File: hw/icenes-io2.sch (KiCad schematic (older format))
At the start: 35 parts, among them J3 Conn_02x11_Odd_Even, J4 Conn_02x31_Odd_Even, J5 Conn_02x31_Odd_Even, U4 iCE40HX8K-CT256

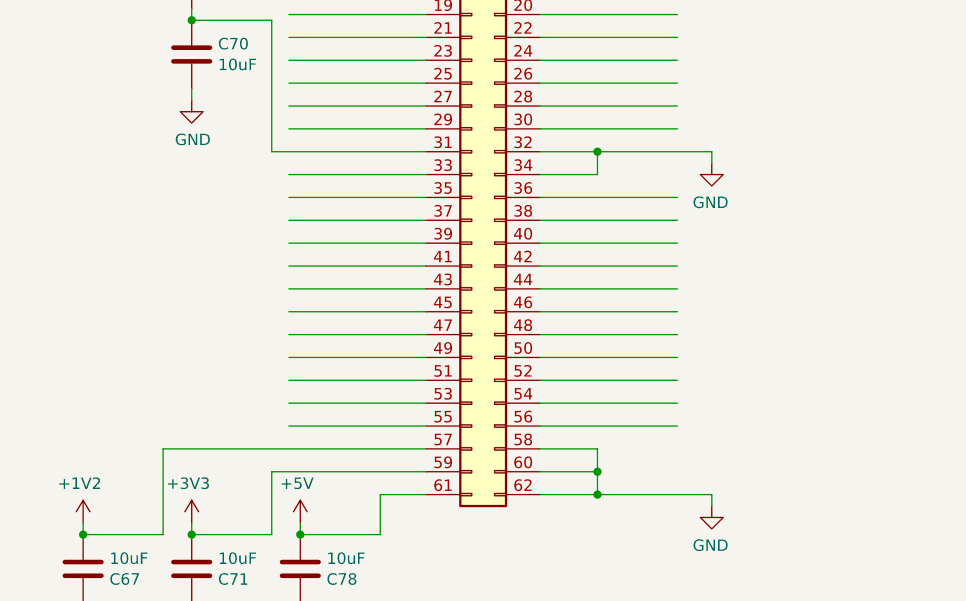
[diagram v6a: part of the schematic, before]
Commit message: Layout. Added some info for the PAL crystal.
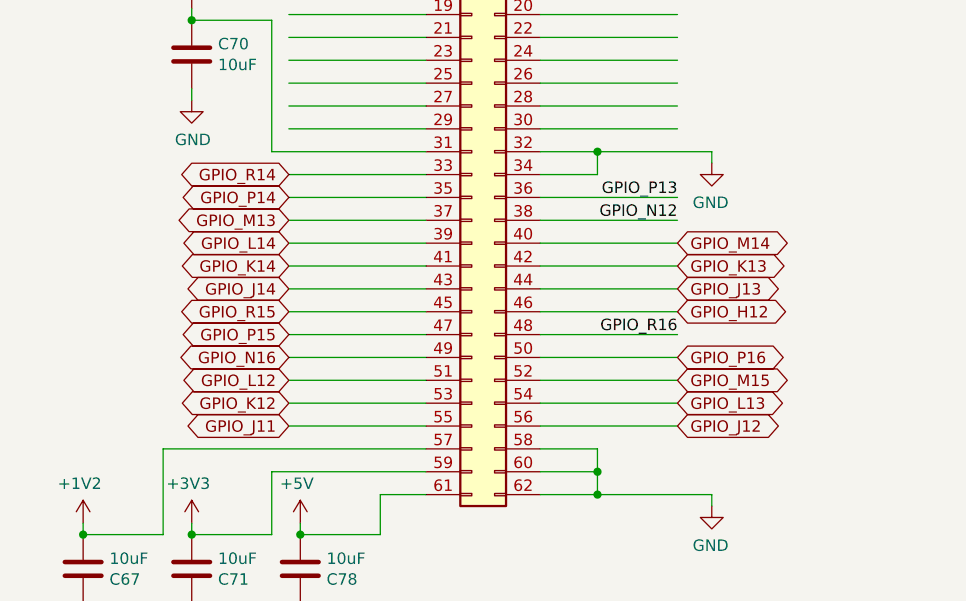
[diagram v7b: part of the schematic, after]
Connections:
- net labels added: GPIO_H12, GPIO_J11, GPIO_J12, GPIO_J13, GPIO_J14, GPIO_K12, GPIO_K13, GPIO_K14, GPIO_L12, GPIO_L13, GPIO_L14, GPIO_M13, GPIO_M14, GPIO_M15, GPIO_N16, GPIO_P14, GPIO_P15, GPIO_P16, GPIO_R14, GPIO_R15
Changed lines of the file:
@@
 Wire Wire Line
 	4400 5500 5000 5500
-Text Label 5000 5500 2    50   ~ 0
-GPIO_R16
 Wire Wire Line
 	11150 1400 11750 1400
@@
 Text GLabel 4550 3100 2    50   Output ~ 0
 DCDn
+Text GLabel 2500 10000 0    50   BiDi ~ 0
+GPIO_J11
+Text GLabel 4200 10000 2    50   BiDi ~ 0
+GPIO_J12
+Text GLabel 2500 9900 0    50   BiDi ~ 0
+GPIO_K12
+Text GLabel 4200 9900 2    50   BiDi ~ 0
+GPIO_L13
+Text GLabel 2500 9800 0    50   BiDi ~ 0
+GPIO_L12
+Text GLabel 4200 9800 2    50   BiDi ~ 0
+GPIO_M15
+Text GLabel 2500 9700 0    50   BiDi ~ 0
+GPIO_N16
+Text GLabel 4200 9700 2    50   BiDi ~ 0
+GPIO_P16
+Text GLabel 2500 9600 0    50   BiDi ~ 0
+GPIO_P15
+Text Label 5000 5500 2    50   ~ 0
+GPIO_R16
+Text Label 4200 9600 2    50   ~ 0
+GPIO_R16
+Text GLabel 2500 9500 0    50   BiDi ~ 0
+GPIO_R15
+Text GLabel 4200 9500 2    50   BiDi ~ 0
+GPIO_H12
+Text GLabel 2500 9400 0    50   BiDi ~ 0
+GPIO_J14
+Text GLabel 4200 9400 2    50   BiDi ~ 0
+GPIO_J13
+Text GLabel 2500 9300 0    50   BiDi ~ 0
+GPIO_K14
+Text GLabel 4200 9300 2    50   BiDi ~ 0
+GPIO_K13
+Text GLabel 2500 9200 0    50   BiDi ~ 0
+GPIO_L14
+Text GLabel 4200 9200 2    50   BiDi ~ 0
+GPIO_M14
+Text GLabel 2500 9100 0    50   BiDi ~ 0
+GPIO_M13
+Text Label 4200 9100 2    50   ~ 0
+GPIO_N12
+Text GLabel 2500 9000 0    50   BiDi ~ 0
+GPIO_P14
+Text Label 4200 9000 2    50   ~ 0
+GPIO_P13
+Text GLabel 2500 8900 0    50   BiDi ~ 0
+GPIO_R14
 $EndSCHEMATC

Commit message: Layout.
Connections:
- net labels added: GPIO_P8, GPIO_P9
- net labels removed: GPIO_T8, GPIO_T9
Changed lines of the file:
@@
 GPIO_T7
 Wire Wire Line
-	4400 3500 5000 3500
-Text Label 5000 3500 2    50   ~ 0
-GPIO_T8
+	4400 4000 5000 4000
+Text Label 5000 4000 2    50   ~ 0
+GPIO_P9
 Wire Wire Line
 	4400 3600 5000 3600
@@
 GPIO_P7
 Wire Wire Line
-	4400 3800 5000 3800
-Text Label 5000 3800 2    50   ~ 0
-GPIO_T9
+	4400 3100 5000 3100
+Text Label 5000 3100 2    50   ~ 0
+GPIO_P8
 Wire Wire Line
 	4400 3900 5000 3900
@@
 Wire Wire Line
 	4400 4500 4550 4500
+Text GLabel 4550 3800 2    50   Input ~ 0
+RTSn
+Wire Wire Line
+	4400 3800 4550 3800
+Wire Wire Line
+	4400 4400 4550 4400
 Text GLabel 4550 4400 2    50   Input ~ 0
-RTSn
-Wire Wire Line
-	4400 4400 4550 4400
+DTRn
 Text GLabel 4550 4300 2    50   Output ~ 0
-CTSn
+DSRn
 Wire Wire Line
 	4400 4300 4550 4300
 Wire Wire Line
 	4400 3700 4550 3700
-Text GLabel 4550 3700 2    50   Input ~ 0
-DTRn
-Text GLabel 4550 4000 2    50   Output ~ 0
-DSRn
-Wire Wire Line
-	4400 4000 4550 4000
-Wire Wire Line
-	4400 3100 4550 3100
-Text GLabel 4550 3100 2    50   Output ~ 0
+Text GLabel 4550 3700 2    50   Output ~ 0
 DCDn
 Text GLabel 2500 10000 0    50   BiDi ~ 0
@@
 Text GLabel 2500 8900 0    50   BiDi ~ 0
 GPIO_R14
+Wire Wire Line
+	4400 3500 4550 3500
+Text GLabel 4550 3500 2    50   Output ~ 0
+CTSn
+Text Label 2500 8600 0    50   ~ 0
+GPIO_T14
+Text Label 4200 8600 2    50   ~ 0
+GPIO_T13
+Text Label 2500 8500 0    50   ~ 0
+GPIO_T11
+Text Label 4200 8500 2    50   ~ 0
+GPIO_L11
+Text Label 4200 8400 2    50   ~ 0
+GPIO_M12
+Text Label 2500 8400 0    50   ~ 0
+GPIO_M11
+Text Label 4200 8300 2    50   ~ 0
+GPIO_L10
+Text Label 2500 8300 0    50   ~ 0
+GPIO_L9
+Text Label 4200 8200 2    50   ~ 0
+GPIO_M9
+Text Label 2500 8700 0    50   ~ 0
+GPIO_T16
+Text Label 4200 8700 2    50   ~ 0
+GPIO_T15
 $EndSCHEMATC
